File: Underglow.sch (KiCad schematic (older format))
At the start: 10 parts

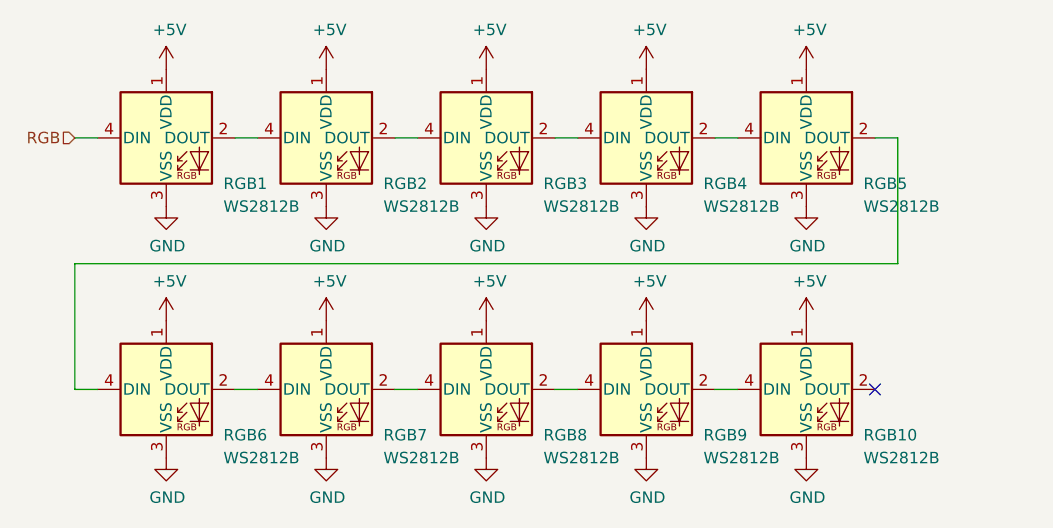
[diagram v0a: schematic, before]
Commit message: Add LCSC part numbers in BOM, fix RGB
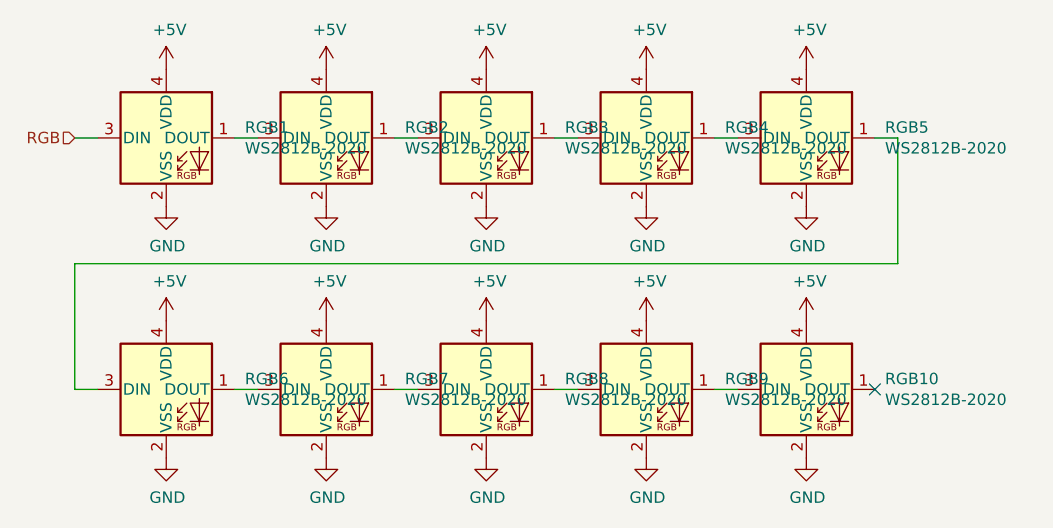
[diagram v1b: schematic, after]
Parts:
- removed RGB1, RGB10, RGB2, RGB3, RGB4, RGB5, RGB6, RGB7, RGB8, RGB9: WS2812B, random-keyboard-parts:WS2812B-2020, symbol LED:WS2812B
- added RGB1, RGB10, RGB2, RGB3, RGB4, RGB5, RGB6, RGB7, RGB8, RGB9: WS2812B-2020, random-keyboard-parts:WS2812B-2020, symbol random-keyboard-parts:WS2812B-2020
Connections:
- net +5V: now also RGB1.4 (VDD), RGB10.4 (VDD), RGB2.4 (VDD), RGB3.4 (VDD), RGB4.4 (VDD), RGB5.4 (VDD), RGB6.4 (VDD), RGB7.4 (VDD), RGB8.4 (VDD), RGB9.4 (VDD)
- net GND: now also RGB1.2 (VSS), RGB10.2 (VSS), RGB2.2 (VSS), RGB3.2 (VSS), RGB4.2 (VSS), RGB5.2 (VSS), RGB6.2 (VSS), RGB7.2 (VSS), RGB8.2 (VSS), RGB9.2 (VSS)
- net RGB: now also RGB1.3 (DIN)
- new net: RGB1.1 (DOUT), RGB2.3 (DIN)
- new net: RGB2.1 (DOUT), RGB3.3 (DIN)
- new net: RGB3.1 (DOUT), RGB4.3 (DIN)
- new net: RGB4.1 (DOUT), RGB5.3 (DIN)
- new net: RGB5.1 (DOUT), RGB6.3 (DIN)
- new net: RGB6.1 (DOUT), RGB7.3 (DIN)
- new net: RGB7.1 (DOUT), RGB8.3 (DIN)
- new net: RGB8.1 (DOUT), RGB9.3 (DIN)
- new net: RGB10.3 (DIN), RGB9.1 (DOUT)
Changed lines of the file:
@@
 $EndDescr
-$Comp
-L LED:WS2812B RGB1
-U 1 1 6235B204
-P 2250 1900
-F 0 "RGB1" H 2500 1700 50  0000 L CNN
-F 1 "WS2812B" H 2500 1600 50  0000 L CNN
-F 2 "random-keyboard-parts:WS2812B-2020" H 2300 1600 50  0001 L TNN
-F 3 "https://cdn-shop.adafruit.com/datasheets/WS2812B.pdf" H 2350 1525 50  0001 L TNN
-	1    2250 1900
-	1    0    0    -1
-$EndComp
 $Comp
 L power:+5V #PWR015
@@
 $EndComp
 $Comp
-L LED:WS2812B RGB2
-U 1 1 6235EA6D
-P 2950 1900
-F 0 "RGB2" H 3200 1700 50  0000 L CNN
-F 1 "WS2812B" H 3200 1600 50  0000 L CNN
-F 2 "random-keyboard-parts:WS2812B-2020" H 3000 1600 50  0001 L TNN
-F 3 "https://cdn-shop.adafruit.com/datasheets/WS2812B.pdf" H 3050 1525 50  0001 L TNN
-	1    2950 1900
-	1    0    0    -1
-$EndComp
-$Comp
 L power:+5V #PWR016
 U 1 1 6235EA73
@@
 $EndComp
 $Comp
-L LED:WS2812B RGB3
-U 1 1 6235F3AC
-P 3650 1900
-F 0 "RGB3" H 3900 1700 50  0000 L CNN
-F 1 "WS2812B" H 3900 1600 50  0000 L CNN
-F 2 "random-keyboard-parts:WS2812B-2020" H 3700 1600 50  0001 L TNN
-F 3 "https://cdn-shop.adafruit.com/datasheets/WS2812B.pdf" H 3750 1525 50  0001 L TNN
-	1    3650 1900
-	1    0    0    -1
-$EndComp
-$Comp
 L power:+5V #PWR017
 U 1 1 6235F3B2
@@
 $EndComp
 $Comp
-L LED:WS2812B RGB4
-U 1 1 623603B1
-P 4350 1900
-F 0 "RGB4" H 4600 1700 50  0000 L CNN
-F 1 "WS2812B" H 4600 1600 50  0000 L CNN
-F 2 "random-keyboard-parts:WS2812B-2020" H 4400 1600 50  0001 L TNN
-F 3 "https://cdn-shop.adafruit.com/datasheets/WS2812B.pdf" H 4450 1525 50  0001 L TNN
-	1    4350 1900
-	1    0    0    -1
-$EndComp
-$Comp
 L power:+5V #PWR018
 U 1 1 623603B7
@@
 $EndComp
 $Comp
-L LED:WS2812B RGB5
-U 1 1 62361174
-P 5050 1900
-F 0 "RGB5" H 5300 1700 50  0000 L CNN
-F 1 "WS2812B" H 5300 1600 50  0000 L CNN
-F 2 "random-keyboard-parts:WS2812B-2020" H 5100 1600 50  0001 L TNN
-F 3 "https://cdn-shop.adafruit.com/datasheets/WS2812B.pdf" H 5150 1525 50  0001 L TNN
-	1    5050 1900
-	1    0    0    -1
-$EndComp
-$Comp
 L power:+5V #PWR019
 U 1 1 6236117A
@@
 $EndComp
 $Comp
-L LED:WS2812B RGB6
-U 1 1 62366AAA
-P 2250 3000
-F 0 "RGB6" H 2500 2800 50  0000 L CNN
-F 1 "WS2812B" H 2500 2700 50  0000 L CNN
-F 2 "random-keyboard-parts:WS2812B-2020" H 2300 2700 50  0001 L TNN
-F 3 "https://cdn-shop.adafruit.com/datasheets/WS2812B.pdf" H 2350 2625 50  0001 L TNN
-	1    2250 3000
-	1    0    0    -1
-$EndComp
-$Comp
 L power:+5V #PWR025
 U 1 1 62366AB0
@@
 $EndComp
 $Comp
-L LED:WS2812B RGB7
-U 1 1 62366ABC
-P 2950 3000
-F 0 "RGB7" H 3200 2800 50  0000 L CNN
-F 1 "WS2812B" H 3200 2700 50  0000 L CNN
-F 2 "random-keyboard-parts:WS2812B-2020" H 3000 2700 50  0001 L TNN
-F 3 "https://cdn-shop.adafruit.com/datasheets/WS2812B.pdf" H 3050 2625 50  0001 L TNN
-	1    2950 3000
-	1    0    0    -1
-$EndComp
-$Comp
 L power:+5V #PWR026
 U 1 1 62366AC2
@@
 $EndComp
 $Comp
-L LED:WS2812B RGB8
-U 1 1 62366ACE
-P 3650 3000
-F 0 "RGB8" H 3900 2800 50  0000 L CNN
-F 1 "WS2812B" H 3900 2700 50  0000 L CNN
-F 2 "random-keyboard-parts:WS2812B-2020" H 3700 2700 50  0001 L TNN
-F 3 "https://cdn-shop.adafruit.com/datasheets/WS2812B.pdf" H 3750 2625 50  0001 L TNN
-	1    3650 3000
-	1    0    0    -1
-$EndComp
-$Comp
 L power:+5V #PWR027
 U 1 1 62366AD4
@@
 $EndComp
 $Comp
-L LED:WS2812B RGB9
-U 1 1 62366AE0
-P 4350 3000
-F 0 "RGB9" H 4600 2800 50  0000 L CNN
-F 1 "WS2812B" H 4600 2700 50  0000 L CNN
-F 2 "random-keyboard-parts:WS2812B-2020" H 4400 2700 50  0001 L TNN
-F 3 "https://cdn-shop.adafruit.com/datasheets/WS2812B.pdf" H 4450 2625 50  0001 L TNN
-	1    4350 3000
-	1    0    0    -1
-$EndComp
-$Comp
 L power:+5V #PWR028
 U 1 1 62366AE6
@@
 $EndComp
 $Comp
-L LED:WS2812B RGB10
-U 1 1 62366AF2
-P 5050 3000
-F 0 "RGB10" H 5300 2800 50  0000 L CNN
-F 1 "WS2812B" H 5300 2700 50  0000 L CNN
-F 2 "random-keyboard-parts:WS2812B-2020" H 5100 2700 50  0001 L TNN
-F 3 "https://cdn-shop.adafruit.com/datasheets/WS2812B.pdf" H 5150 2625 50  0001 L TNN
-	1    5050 3000
-	1    0    0    -1
-$EndComp
-$Comp
 L power:+5V #PWR029
 U 1 1 62366AF8
@@
 	4650 3000 4750 3000
 NoConn ~ 5350 3000
+$Comp
+L random-keyboard-parts:WS2812B-2020 RGB1
+U 1 1 63F5DC33
+P 2250 1900
+F 0 "RGB1" H 2594 1946 50  0000 L CNN
+F 1 "WS2812B-2020" H 2594 1855 50  0000 L CNN
+F 2 "random-keyboard-parts:WS2812B-2020" H 2300 1600 50  0001 L TNN
+F 3 "https://cdn-shop.adafruit.com/datasheets/WS2812B.pdf" H 2350 1525 50  0001 L TNN
+F 4 "C965555" H 2250 1900 50  0001 C CNN "LCSC"
+	1    2250 1900
+	1    0    0    -1
+$EndComp
+$Comp
+L random-keyboard-parts:WS2812B-2020 RGB2
+U 1 1 63F5E4B7
+P 2950 1900
+F 0 "RGB2" H 3294 1946 50  0000 L CNN
+F 1 "WS2812B-2020" H 3294 1855 50  0000 L CNN
+F 2 "random-keyboard-parts:WS2812B-2020" H 3000 1600 50  0001 L TNN
+F 3 "https://cdn-shop.adafruit.com/datasheets/WS2812B.pdf" H 3050 1525 50  0001 L TNN
+F 4 "C965555" H 2950 1900 50  0001 C CNN "LCSC"
+	1    2950 1900
+	1    0    0    -1
+$EndComp
+$Comp
+L random-keyboard-parts:WS2812B-2020 RGB3
+U 1 1 63F5E975
+P 3650 1900
+F 0 "RGB3" H 3994 1946 50  0000 L CNN
+F 1 "WS2812B-2020" H 3994 1855 50  0000 L CNN
+F 2 "random-keyboard-parts:WS2812B-2020" H 3700 1600 50  0001 L TNN
+F 3 "https://cdn-shop.adafruit.com/datasheets/WS2812B.pdf" H 3750 1525 50  0001 L TNN
+F 4 "C965555" H 3650 1900 50  0001 C CNN "LCSC"
+	1    3650 1900
+	1    0    0    -1
+$EndComp
+$Comp
+L random-keyboard-parts:WS2812B-2020 RGB4
+U 1 1 63F5EE6B
+P 4350 1900
+F 0 "RGB4" H 4694 1946 50  0000 L CNN
+F 1 "WS2812B-2020" H 4694 1855 50  0000 L CNN
+F 2 "random-keyboard-parts:WS2812B-2020" H 4400 1600 50  0001 L TNN
+F 3 "https://cdn-shop.adafruit.com/datasheets/WS2812B.pdf" H 4450 1525 50  0001 L TNN
+F 4 "C965555" H 4350 1900 50  0001 C CNN "LCSC"
+	1    4350 1900
+	1    0    0    -1
+$EndComp
+$Comp
+L random-keyboard-parts:WS2812B-2020 RGB5
+U 1 1 63F5F28D
+P 5050 1900
+F 0 "RGB5" H 5394 1946 50  0000 L CNN
+F 1 "WS2812B-2020" H 5394 1855 50  0000 L CNN
+F 2 "random-keyboard-parts:WS2812B-2020" H 5100 1600 50  0001 L TNN
+F 3 "https://cdn-shop.adafruit.com/datasheets/WS2812B.pdf" H 5150 1525 50  0001 L TNN
+F 4 "C965555" H 5050 1900 50  0001 C CNN "LCSC"
+	1    5050 1900
+	1    0    0    -1
+$EndComp
+$Comp
+L random-keyboard-parts:WS2812B-2020 RGB6
+U 1 1 63F5F73D
+P 2250 3000
+F 0 "RGB6" H 2594 3046 50  0000 L CNN
+F 1 "WS2812B-2020" H 2594 2955 50  0000 L CNN
+F 2 "random-keyboard-parts:WS2812B-2020" H 2300 2700 50  0001 L TNN
+F 3 "https://cdn-shop.adafruit.com/datasheets/WS2812B.pdf" H 2350 2625 50  0001 L TNN
+F 4 "C965555" H 2250 3000 50  0001 C CNN "LCSC"
+	1    2250 3000
+	1    0    0    -1
+$EndComp
+$Comp
+L random-keyboard-parts:WS2812B-2020 RGB7
+U 1 1 63F5FF00
+P 2950 3000
+F 0 "RGB7" H 3294 3046 50  0000 L CNN
+F 1 "WS2812B-2020" H 3294 2955 50  0000 L CNN
+F 2 "random-keyboard-parts:WS2812B-2020" H 3000 2700 50  0001 L TNN
+F 3 "https://cdn-shop.adafruit.com/datasheets/WS2812B.pdf" H 3050 2625 50  0001 L TNN
+F 4 "C965555" H 2950 3000 50  0001 C CNN "LCSC"
+	1    2950 3000
+	1    0    0    -1
+$EndComp
+$Comp
+L random-keyboard-parts:WS2812B-2020 RGB8
+U 1 1 63F604FB
+P 3650 3000
+F 0 "RGB8" H 3994 3046 50  0000 L CNN
+F 1 "WS2812B-2020" H 3994 2955 50  0000 L CNN
+F 2 "random-keyboard-parts:WS2812B-2020" H 3700 2700 50  0001 L TNN
+F 3 "https://cdn-shop.adafruit.com/datasheets/WS2812B.pdf" H 3750 2625 50  0001 L TNN
+F 4 "C965555" H 3650 3000 50  0001 C CNN "LCSC"
+	1    3650 3000
+	1    0    0    -1
+$EndComp
+$Comp
+L random-keyboard-parts:WS2812B-2020 RGB9
+U 1 1 63F60B2E
+P 4350 3000
+F 0 "RGB9" H 4694 3046 50  0000 L CNN
+F 1 "WS2812B-2020" H 4694 2955 50  0000 L CNN
+F 2 "random-keyboard-parts:WS2812B-2020" H 4400 2700 50  0001 L TNN
+F 3 "https://cdn-shop.adafruit.com/datasheets/WS2812B.pdf" H 4450 2625 50  0001 L TNN
+F 4 "C965555" H 4350 3000 50  0001 C CNN "LCSC"
+	1    4350 3000
+	1    0    0    -1
+$EndComp
+$Comp
+L random-keyboard-parts:WS2812B-2020 RGB10
+U 1 1 63F60FE7
+P 5050 3000
+F 0 "RGB10" H 5394 3046 50  0000 L CNN
+F 1 "WS2812B-2020" H 5394 2955 50  0000 L CNN
+F 2 "random-keyboard-parts:WS2812B-2020" H 5100 2700 50  0001 L TNN
+F 3 "https://cdn-shop.adafruit.com/datasheets/WS2812B.pdf" H 5150 2625 50  0001 L TNN
+F 4 "C965555" H 5050 3000 50  0001 C CNN "LCSC"
+	1    5050 3000
+	1    0    0    -1
+$EndComp
 $EndSCHEMATC
